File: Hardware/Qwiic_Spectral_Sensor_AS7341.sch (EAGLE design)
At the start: 21 parts, among them J1 QWIIC_RIGHT_ANGLE, J3 QWIIC_RIGHT_ANGLE, U1 MLX90614

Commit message: Working on schematic
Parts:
- removed R5: 2.2k, SparkFun-Resistors:2.2KOHM-0603-1/10W-1%
- added C2: 0.1uF, SparkFun-Capacitors:0.1UF-0603-25V-(+80/-20%)
- added C3, C4: 1.0uF, SparkFun-Capacitors:1.0UF-0603-16V-10%
- added D2: White, 60mA, SparkFun-LED:LED-WHITE3014
- added D3: LED-IR0603, SparkFun-LED:LED-IR0603
- added D4, D5: (no value), SparkFun-LED:LED-3MM-NO_SILK
- added JP3, JP4: JUMPER-SMT_2_NC_TRACE_SILK, SparkFun-Jumpers:JUMPER-SMT_2_NC_TRACE_SILK
- added R1: 2.2k, SparkFun-Resistors:2.2KOHM-0603-1/10W-1%
- added U2: PCA9536, New_Parts:PCA9536
- added U3: AP2127K-1.8V, SparkFun-IC-Power:V_REG_AP2127K-1.8V
- C1: value 0.1uF -> 10uF; device SparkFun-Capacitors:0.1UF-0603-25V-5% -> SparkFun-Capacitors:10UF-0603-6.3V-20%
- U1: value MLX90614 -> AS7341OLGA; device SparkFun-Sensors:MLX90614 -> AS7341:AS7341OLGA
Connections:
- new net 1.8V: C4.1, U1.VDD, U3.OUT
- new net GPIO0: U2.GPIO0
- new net GPIO1: U2.GPIO1
- new net GPIO2: U2.GPIO2
- new net GPIO3: U2.GPIO3
- new net LDR: D2.C, D3.C, D4.C, D5.C, U1.LDR
- new net N$5: D2.A, JP4.1
- new net N$6: U3.EN, U3.IN
- new net N$7: D3.A, JP3.1
- net 3.3V: now also C2.1, C3.1, U2.VCC; no longer U1.VDD
- net GND: now also C2.2, C3.2, C4.2, U1.GND, U1.PGND, U2.GND, U3.GND; no longer U1.VSS
- net N$1: now also JP1.3, R1.1; no longer JP1.1, R2.2
- net N$3: now also JP1.1, R2.1; no longer JP1.3, R5.2
- net SCL: now also R2.2, U1.SCL, U2.SCL; no longer R2.1, U1.SCL/VZ
- net SDA: now also R1.2, U1.SDA, U2.SDA; no longer R5.1, U1.SDA/PWM
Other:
- note added: "4-bit GPIO"
- note added: "Default I2C Address: 0x39"
- note added: "Default I2C Address: 0x41"
- note added: "I2C pullup resistors"
- note added: "Spectral Sensor - AS7341"
- note added: "Voltage Regulator"
- note removed: "Default I2C Address: 0x5A"
- note removed: "I2C Pullup Resistors"
- note removed: "IR Thermometer - MLX90614"
- moved on the sheet: C1, D1, J1, J2, J3, JP1, JP2, R2, R3

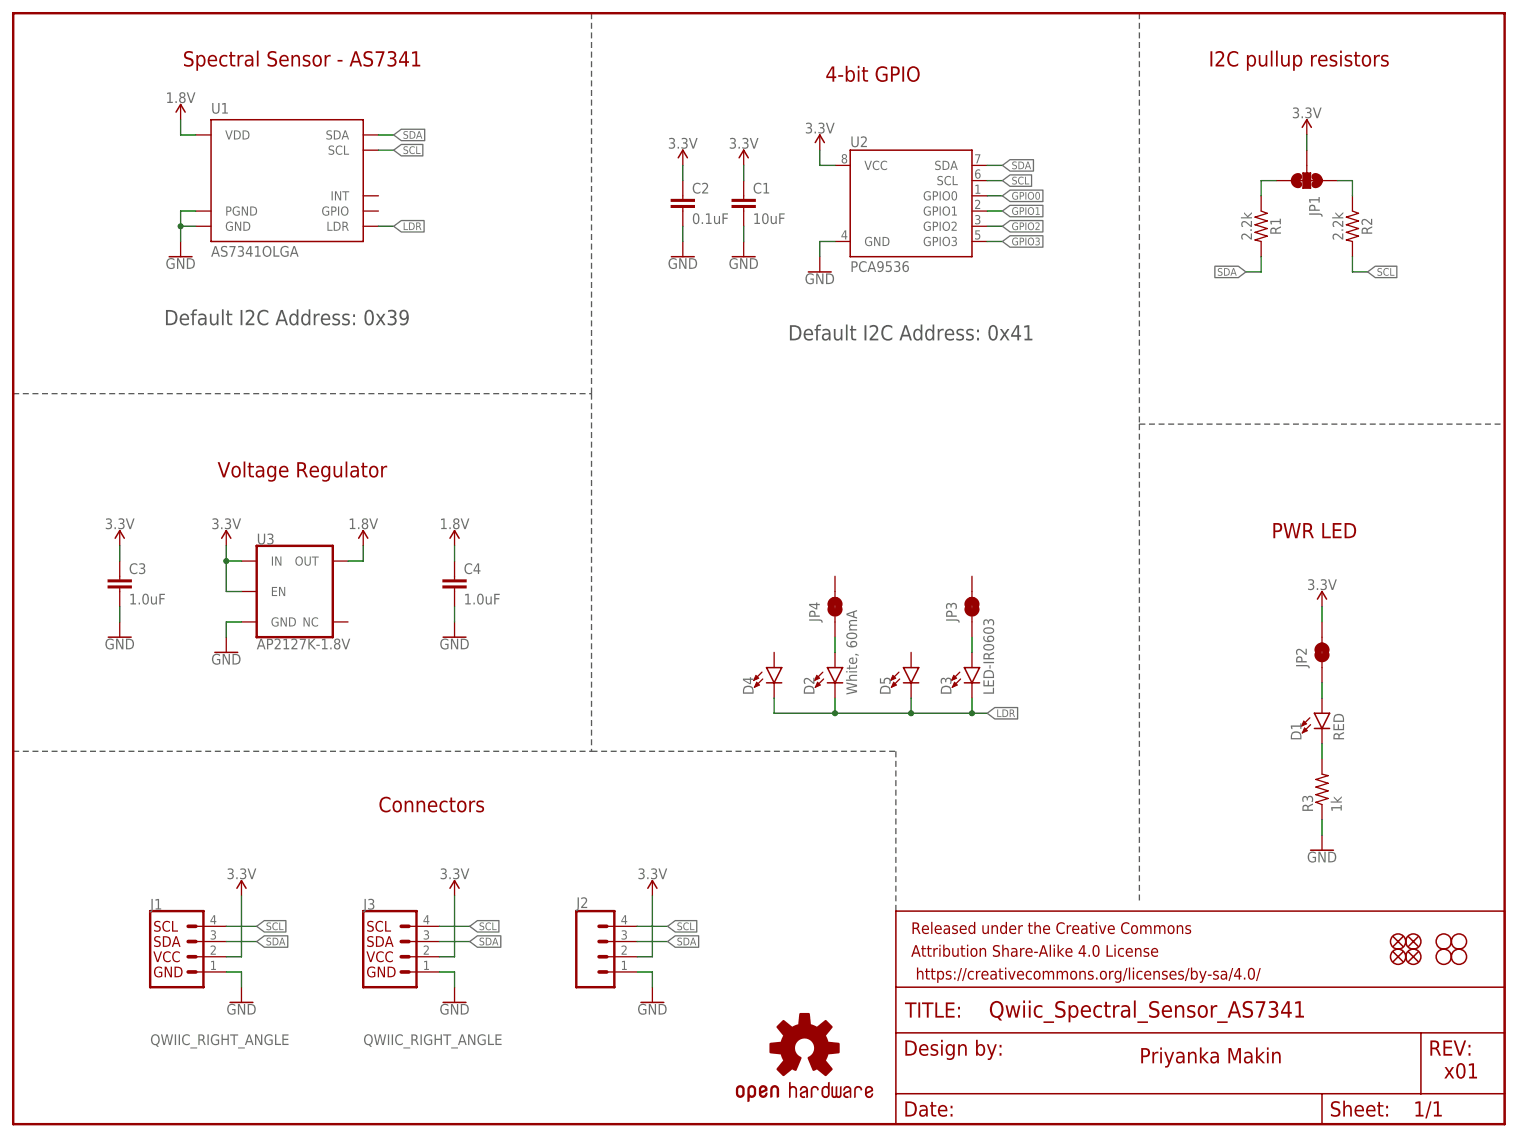
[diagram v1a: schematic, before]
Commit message: First draft of schematic finished
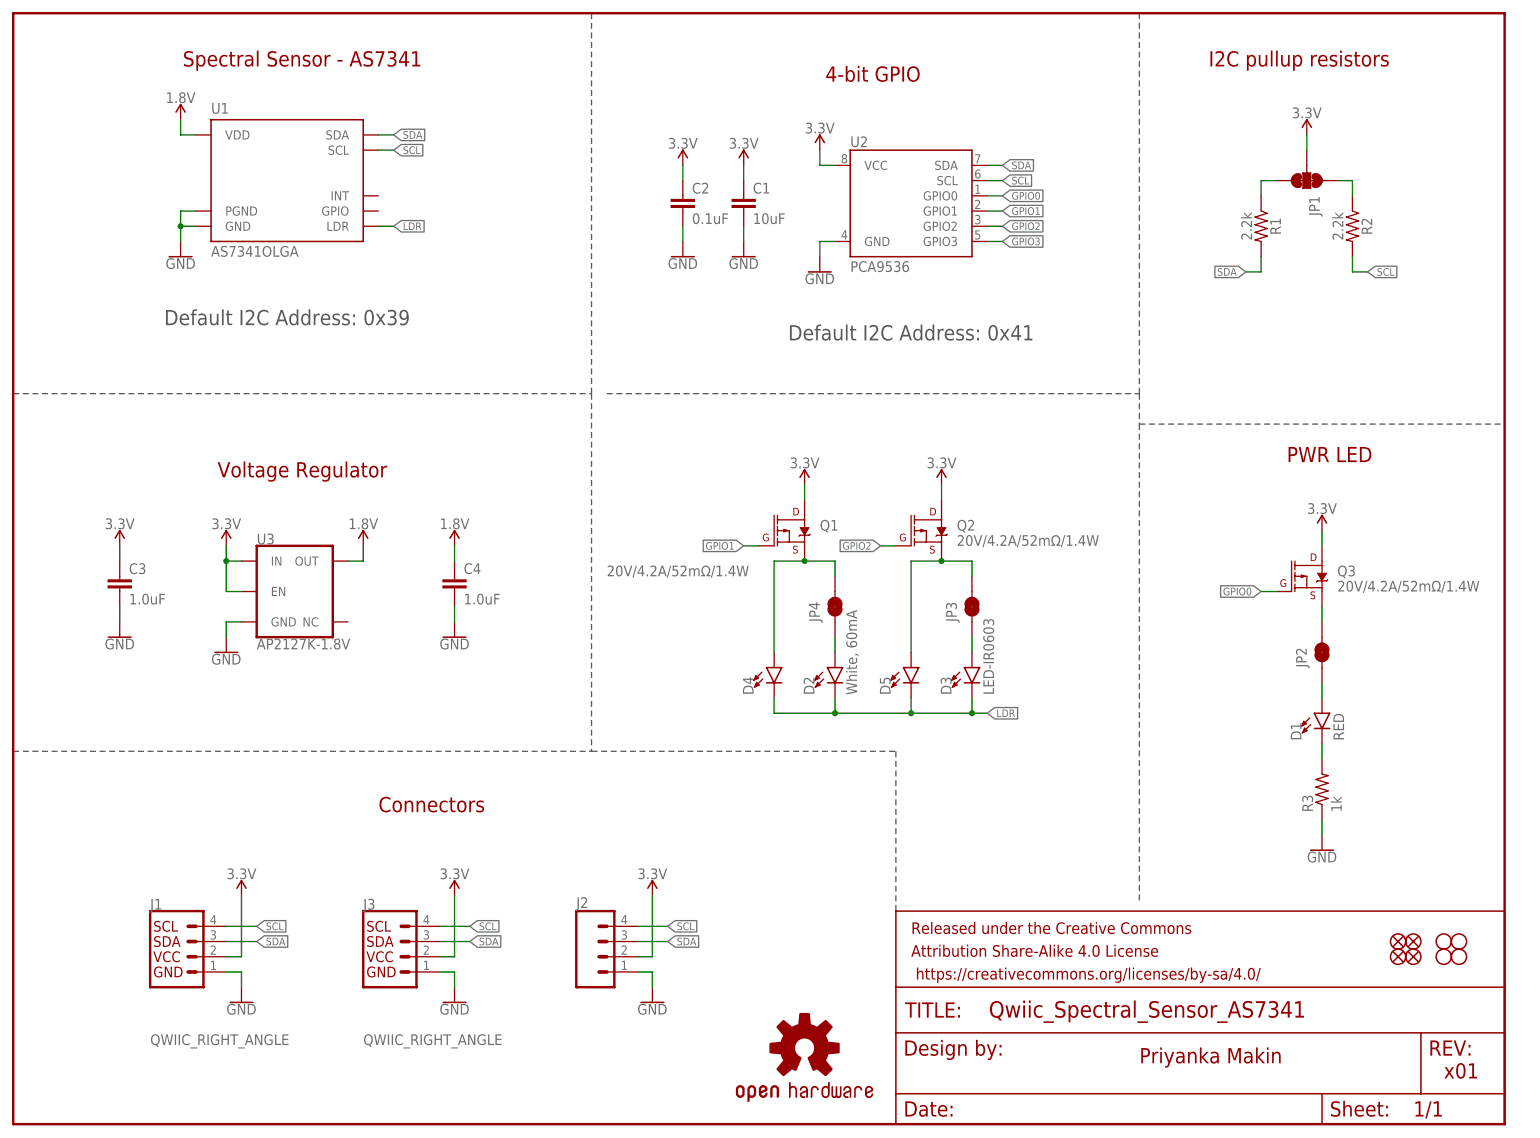
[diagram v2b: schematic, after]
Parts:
- added Q1, Q2, Q3: 20V/4.2A/52mΩ/1.4W, SparkFun-DiscreteSemi:MOSFET_PCH-DMG2305UX-7
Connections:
- new net N$10: JP2.2, Q3.S
- new net N$8: D4.A, JP4.2, Q1.S
- new net N$9: D5.A, JP3.2, Q2.S
- net 3.3V: now also Q1.D, Q2.D, Q3.D; no longer JP2.2
- net GPIO0: now also Q3.G
- net GPIO1: now also Q1.G
- net GPIO2: now also Q2.G
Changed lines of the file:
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@@
 <part name="H3" library="SparkFun-Hardware" deviceset="STAND-OFF" device=""/>
 <part name="H4" library="SparkFun-Hardware" deviceset="STAND-OFF" device=""/>
-<part name="SUPPLY6" library="SparkFun-PowerSymbols" deviceset="3.3V" device=""/>
 <part name="GND5" library="SparkFun-PowerSymbols" deviceset="GND" device=""/>
 <part name="U1" library="AS7341" deviceset="AS7341" device="OLGA"/>
@@
 <part name="JP3" library="SparkFun-Jumpers" deviceset="JUMPER-SMT_2_NC_TRACE" device="_SILK" package3d_urn="urn:adsk.eagle:package:39281/1"/>
 <part name="JP4" library="SparkFun-Jumpers" deviceset="JUMPER-SMT_2_NC_TRACE" device="_SILK" package3d_urn="urn:adsk.eagle:package:39281/1"/>
+<part name="Q1" library="SparkFun-DiscreteSemi" deviceset="MOSFET_PCH" device="-DMG2305UX-7" value="20V/4.2A/52mΩ/1.4W"/>
+<part name="Q2" library="SparkFun-DiscreteSemi" deviceset="MOSFET_PCH" device="-DMG2305UX-7" value="20V/4.2A/52mΩ/1.4W"/>
+<part name="SUPPLY14" library="SparkFun-PowerSymbols" deviceset="3.3V" device=""/>
+<part name="SUPPLY15" library="SparkFun-PowerSymbols" deviceset="3.3V" device=""/>
+<part name="Q3" library="SparkFun-DiscreteSemi" deviceset="MOSFET_PCH" device="-DMG2305UX-7" value="20V/4.2A/52mΩ/1.4W"/>
+<part name="SUPPLY6" library="SparkFun-PowerSymbols" deviceset="3.3V" device=""/>
 </parts>
 <sheets>
@@
 <wire x1="96.52" y1="185.42" x2="96.52" y2="121.92" width="0.2032" layer="97" style="longdash"/>
 <wire x1="96.52" y1="121.92" x2="96.52" y2="62.23" width="0.2032" layer="97" style="longdash"/>
-<wire x1="187.96" y1="185.42" x2="187.96" y2="116.84" width="0.2032" layer="97" style="longdash"/>
+<wire x1="187.96" y1="185.42" x2="187.96" y2="124.46" width="0.2032" layer="97" style="longdash"/>
 <text x="69.85" y="53.34" size="2.54" layer="94" align="center">Connectors</text>
 <text x="48.26" y="177.8" size="2.54" layer="94" align="center">Spectral Sensor - AS7341</text>
 <text x="143.51" y="175.26" size="2.54" layer="94" align="center">4-bit GPIO</text>
-<text x="217.17" y="99.06" size="2.54" layer="94" align="center">PWR LED</text>
+<text x="219.71" y="111.76" size="2.54" layer="94" align="center">PWR LED</text>
 <text x="45.72" y="134.62" size="2.54" layer="97" align="center">Default I2C Address: 0x39</text>
 <text x="149.86" y="132.08" size="2.54" layer="97" align="center">Default I2C Address: 0x41</text>
 <text x="214.63" y="177.8" size="2.54" layer="94" align="center">I2C pullup resistors</text>
 <text x="48.26" y="109.22" size="2.54" layer="94" align="center">Voltage Regulator</text>
+<wire x1="187.96" y1="121.92" x2="187.96" y2="116.84" width="0.2032" layer="97" style="longdash"/>
 <wire x1="187.96" y1="116.84" x2="187.96" y2="36.83" width="0.2032" layer="97" style="longdash"/>
 <wire x1="0" y1="121.92" x2="96.52" y2="121.92" width="0.2032" layer="97" style="longdash"/>
 <wire x1="187.96" y1="116.84" x2="248.92" y2="116.84" width="0.2032" layer="97" style="longdash"/>
+<wire x1="99.06" y1="121.92" x2="187.96" y2="121.92" width="0.2032" layer="97" style="longdash"/>
+<wire x1="187.96" y1="121.92" x2="187.96" y2="124.46" width="0.2032" layer="97" style="longdash"/>
 </plain>
 <instances>
@@
 <instance part="H3" gate="G$1" x="241.3" y="27.94" smashed="yes"/>
 <instance part="H4" gate="G$1" x="238.76" y="27.94" smashed="yes"/>
-<instance part="SUPPLY6" gate="G$1" x="218.44" y="86.36" smashed="yes">
-<attribute name="VALUE" x="218.44" y="89.154" size="1.778" layer="96" align="bottom-center"/>
-</instance>
 <instance part="GND5" gate="1" x="218.44" y="45.72" smashed="yes">
 <attribute name="VALUE" x="218.44" y="45.466" size="1.778" layer="96" align="top-center"/>
@@
 <instance part="JP4" gate="G$1" x="137.16" y="86.36" smashed="yes" rot="R90">
 <attribute name="NAME" x="134.62" y="83.82" size="1.778" layer="95" font="vector" rot="R90"/>
+</instance>
+<instance part="Q1" gate="G$1" x="129.54" y="99.06" smashed="yes">
+<attribute name="NAME" x="134.62" y="99.06" size="1.778" layer="95" font="vector"/>
+<attribute name="VALUE" x="99.06" y="91.44" size="1.778" layer="96" font="vector"/>
+</instance>
+<instance part="Q2" gate="G$1" x="152.4" y="99.06" smashed="yes">
+<attribute name="NAME" x="157.48" y="99.06" size="1.778" layer="95" font="vector"/>
+<attribute name="VALUE" x="157.48" y="96.52" size="1.778" layer="96" font="vector"/>
+</instance>
+<instance part="SUPPLY14" gate="G$1" x="132.08" y="106.68" smashed="yes">
+<attribute name="VALUE" x="132.08" y="109.474" size="1.778" layer="96" align="bottom-center"/>
+</instance>
+<instance part="SUPPLY15" gate="G$1" x="154.94" y="106.68" smashed="yes">
+<attribute name="VALUE" x="154.94" y="109.474" size="1.778" layer="96" align="bottom-center"/>
+</instance>
+<instance part="Q3" gate="G$1" x="215.9" y="91.44" smashed="yes">
+<attribute name="NAME" x="220.98" y="91.44" size="1.778" layer="95" font="vector"/>
+<attribute name="VALUE" x="220.98" y="88.9" size="1.778" layer="96" font="vector"/>
+</instance>
+<instance part="SUPPLY6" gate="G$1" x="218.44" y="99.06" smashed="yes">
+<attribute name="VALUE" x="218.44" y="101.854" size="1.778" layer="96" align="bottom-center"/>
 </instance>
 </instances>
@@
 </segment>
 <segment>
-<pinref part="JP2" gate="G$1" pin="2"/>
-<wire x1="218.44" y1="86.36" x2="218.44" y2="83.82" width="0.1524" layer="91"/>
-<pinref part="SUPPLY6" gate="G$1" pin="3.3V"/>
-</segment>
-<segment>
 <pinref part="U2" gate="U1" pin="VCC"/>
 <wire x1="137.16" y1="160.02" x2="134.62" y2="160.02" width="0.1524" layer="91"/>
@@
 <wire x1="17.78" y1="93.98" x2="17.78" y2="96.52" width="0.1524" layer="91"/>
 <pinref part="SUPPLY12" gate="G$1" pin="3.3V"/>
+</segment>
+<segment>
+<pinref part="Q1" gate="G$1" pin="D"/>
+<wire x1="132.08" y1="104.14" x2="132.08" y2="106.68" width="0.1524" layer="91"/>
+<pinref part="SUPPLY14" gate="G$1" pin="3.3V"/>
+</segment>
+<segment>
+<pinref part="Q2" gate="G$1" pin="D"/>
+<wire x1="154.94" y1="104.14" x2="154.94" y2="106.68" width="0.1524" layer="91"/>
+<pinref part="SUPPLY15" gate="G$1" pin="3.3V"/>
+</segment>
+<segment>
+<pinref part="Q3" gate="G$1" pin="D"/>
+<wire x1="218.44" y1="96.52" x2="218.44" y2="99.06" width="0.1524" layer="91"/>
+<pinref part="SUPPLY6" gate="G$1" pin="3.3V"/>
 </segment>
 </net>
@@
 <label x="165.1" y="154.94" size="1.27" layer="95" xref="yes"/>
 </segment>
+<segment>
+<pinref part="Q3" gate="G$1" pin="G"/>
+<wire x1="210.82" y1="88.9" x2="208.28" y2="88.9" width="0.1524" layer="91"/>
+<label x="208.28" y="88.9" size="1.27" layer="95" rot="R180" xref="yes"/>
+</segment>
 </net>
 <net name="GPIO1" class="0">
@@
 <label x="165.1" y="152.4" size="1.27" layer="95" xref="yes"/>
 </segment>
+<segment>
+<pinref part="Q1" gate="G$1" pin="G"/>
+<wire x1="124.46" y1="96.52" x2="121.92" y2="96.52" width="0.1524" layer="91"/>
+<label x="121.92" y="96.52" size="1.27" layer="95" rot="R180" xref="yes"/>
+</segment>
 </net>
 <net name="GPIO2" class="0">
@@
 <wire x1="162.56" y1="149.86" x2="165.1" y2="149.86" width="0.1524" layer="91"/>
 <label x="165.1" y="149.86" size="1.27" layer="95" xref="yes"/>
+</segment>
+<segment>
+<pinref part="Q2" gate="G$1" pin="G"/>
+<wire x1="147.32" y1="96.52" x2="144.78" y2="96.52" width="0.1524" layer="91"/>
+<label x="144.78" y="96.52" size="1.27" layer="95" rot="R180" xref="yes"/>
 </segment>
 </net>
@@
 </segment>
 </net>
+<net name="N$8" class="0">
+<segment>
+<pinref part="D4" gate="D1" pin="A"/>
+<wire x1="127" y1="78.74" x2="127" y2="93.98" width="0.1524" layer="91"/>
+<pinref part="Q1" gate="G$1" pin="S"/>
+<wire x1="127" y1="93.98" x2="132.08" y2="93.98" width="0.1524" layer="91"/>
+<wire x1="132.08" y1="93.98" x2="137.16" y2="93.98" width="0.1524" layer="91"/>
+<junction x="132.08" y="93.98"/>
+<pinref part="JP4" gate="G$1" pin="2"/>
+<wire x1="137.16" y1="93.98" x2="137.16" y2="91.44" width="0.1524" layer="91"/>
+</segment>
+</net>
+<net name="N$9" class="0">
+<segment>
+<pinref part="D5" gate="D1" pin="A"/>
+<pinref part="Q2" gate="G$1" pin="S"/>
+<wire x1="149.86" y1="78.74" x2="149.86" y2="93.98" width="0.1524" layer="91"/>
+<wire x1="149.86" y1="93.98" x2="154.94" y2="93.98" width="0.1524" layer="91"/>
+<wire x1="154.94" y1="93.98" x2="160.02" y2="93.98" width="0.1524" layer="91"/>
+<junction x="154.94" y="93.98"/>
+<pinref part="JP3" gate="G$1" pin="2"/>
+<wire x1="160.02" y1="93.98" x2="160.02" y2="91.44" width="0.1524" layer="91"/>
+</segment>
+</net>
+<net name="N$10" class="0">
+<segment>
+<pinref part="JP2" gate="G$1" pin="2"/>
+<pinref part="Q3" gate="G$1" pin="S"/>
+<wire x1="218.44" y1="83.82" x2="218.44" y2="86.36" width="0.1524" layer="91"/>
+</segment>
+</net>

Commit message: Added int pin to schematic
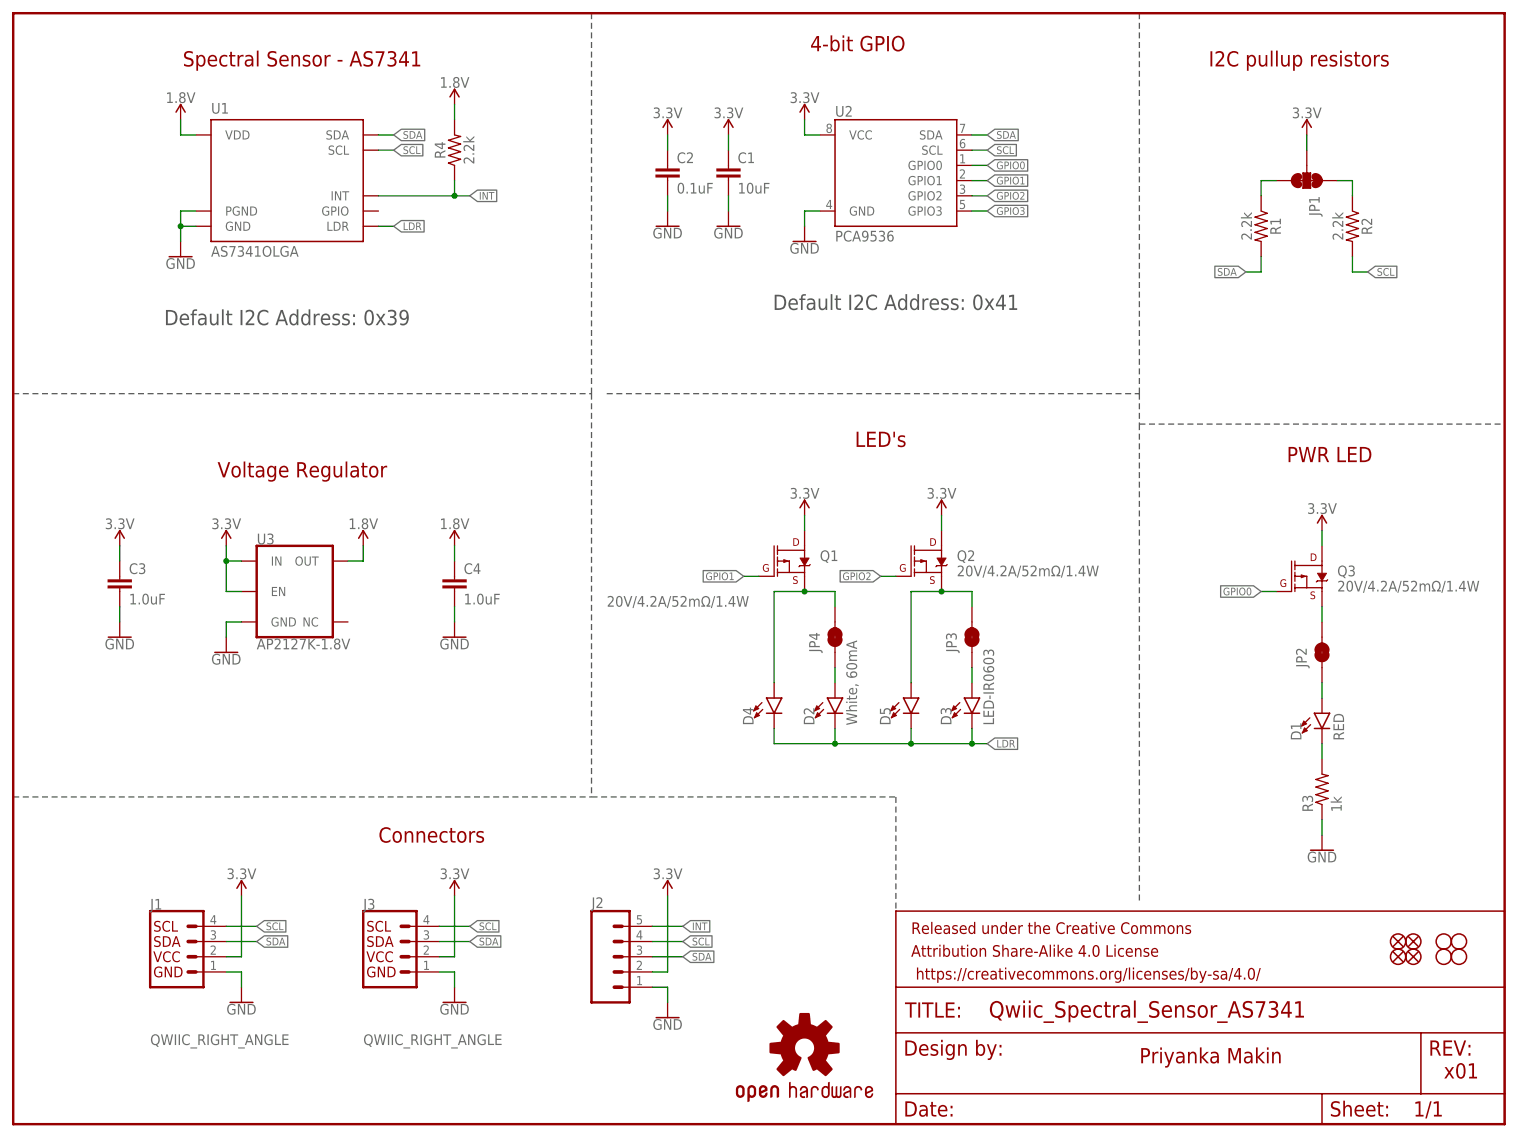
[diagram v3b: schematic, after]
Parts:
- added R4: 2.2k, SparkFun-Resistors:2.2KOHM-0603-1/10W-1%
- J2: device SparkFun-Connectors:CONN_041X04_NO_SILK_NO_POP -> SparkFun-Connectors:CONN_05NO_SILK
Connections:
- new net INT: J2.5, R4.1, U1.INT
- net 1.8V: now also R4.2
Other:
- note added: "LED's"
- moved on the sheet: C1, C2, D2, D3, D4, D5, JP3, JP4, Q1, Q2, U2
